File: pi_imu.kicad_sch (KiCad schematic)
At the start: 4 parts, among them J8 430450212, U10 4754, U6 MAX485, U8 RASPBERRY_PI_4B_4GB

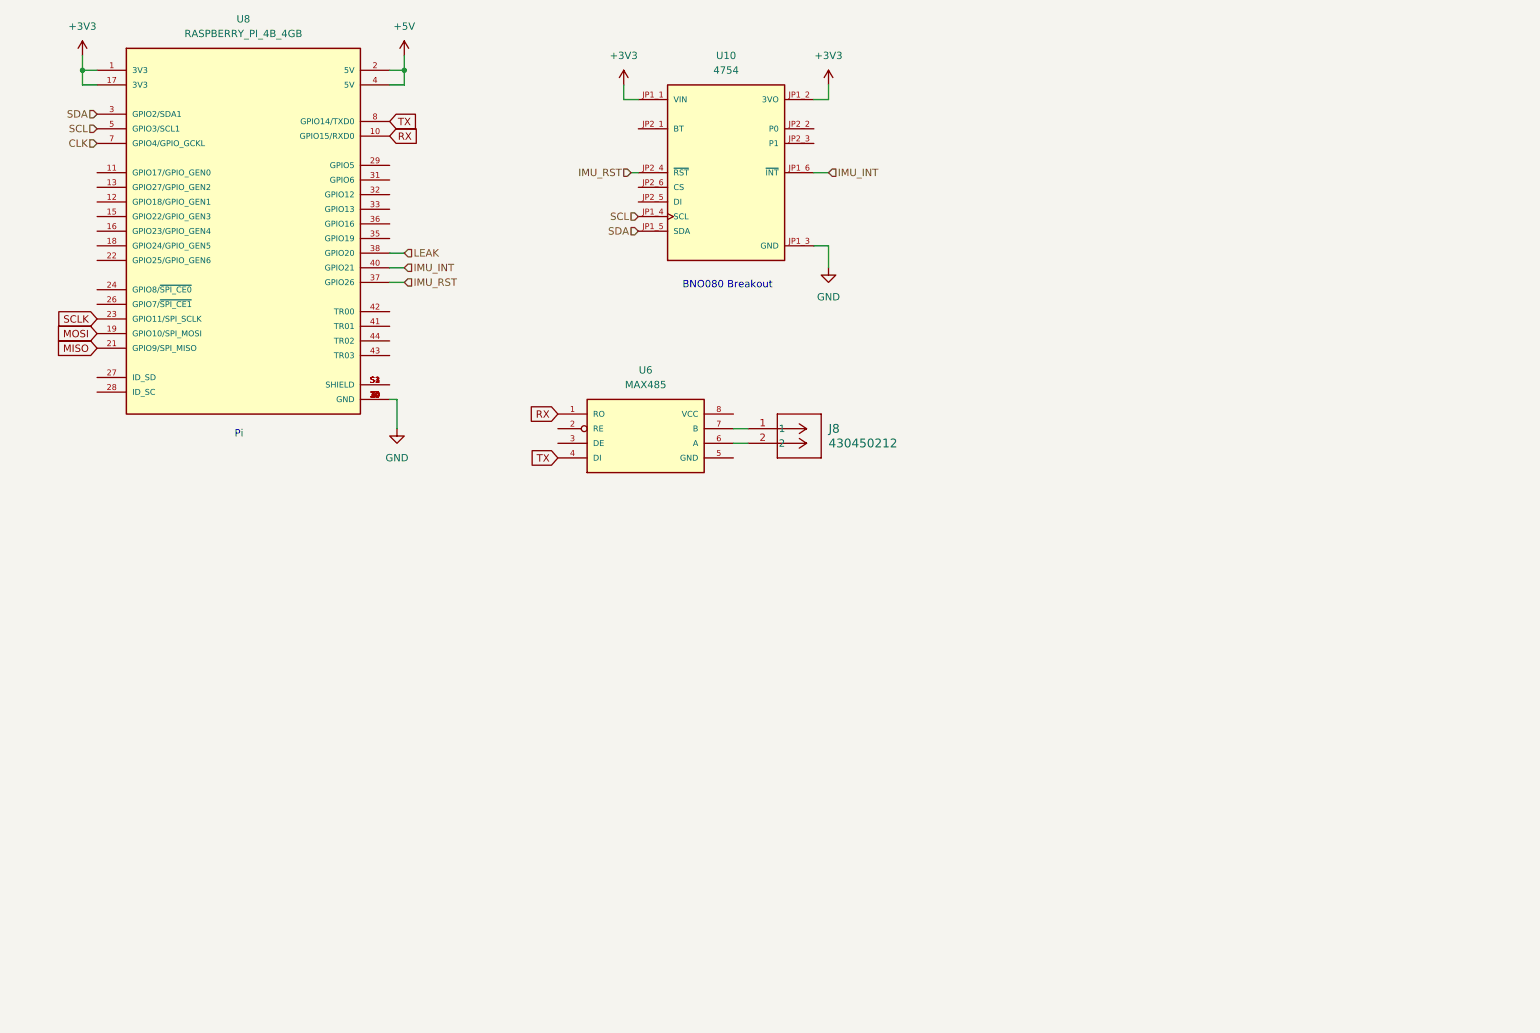
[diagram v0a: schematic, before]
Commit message: Added New Libraries and Schematic Updates
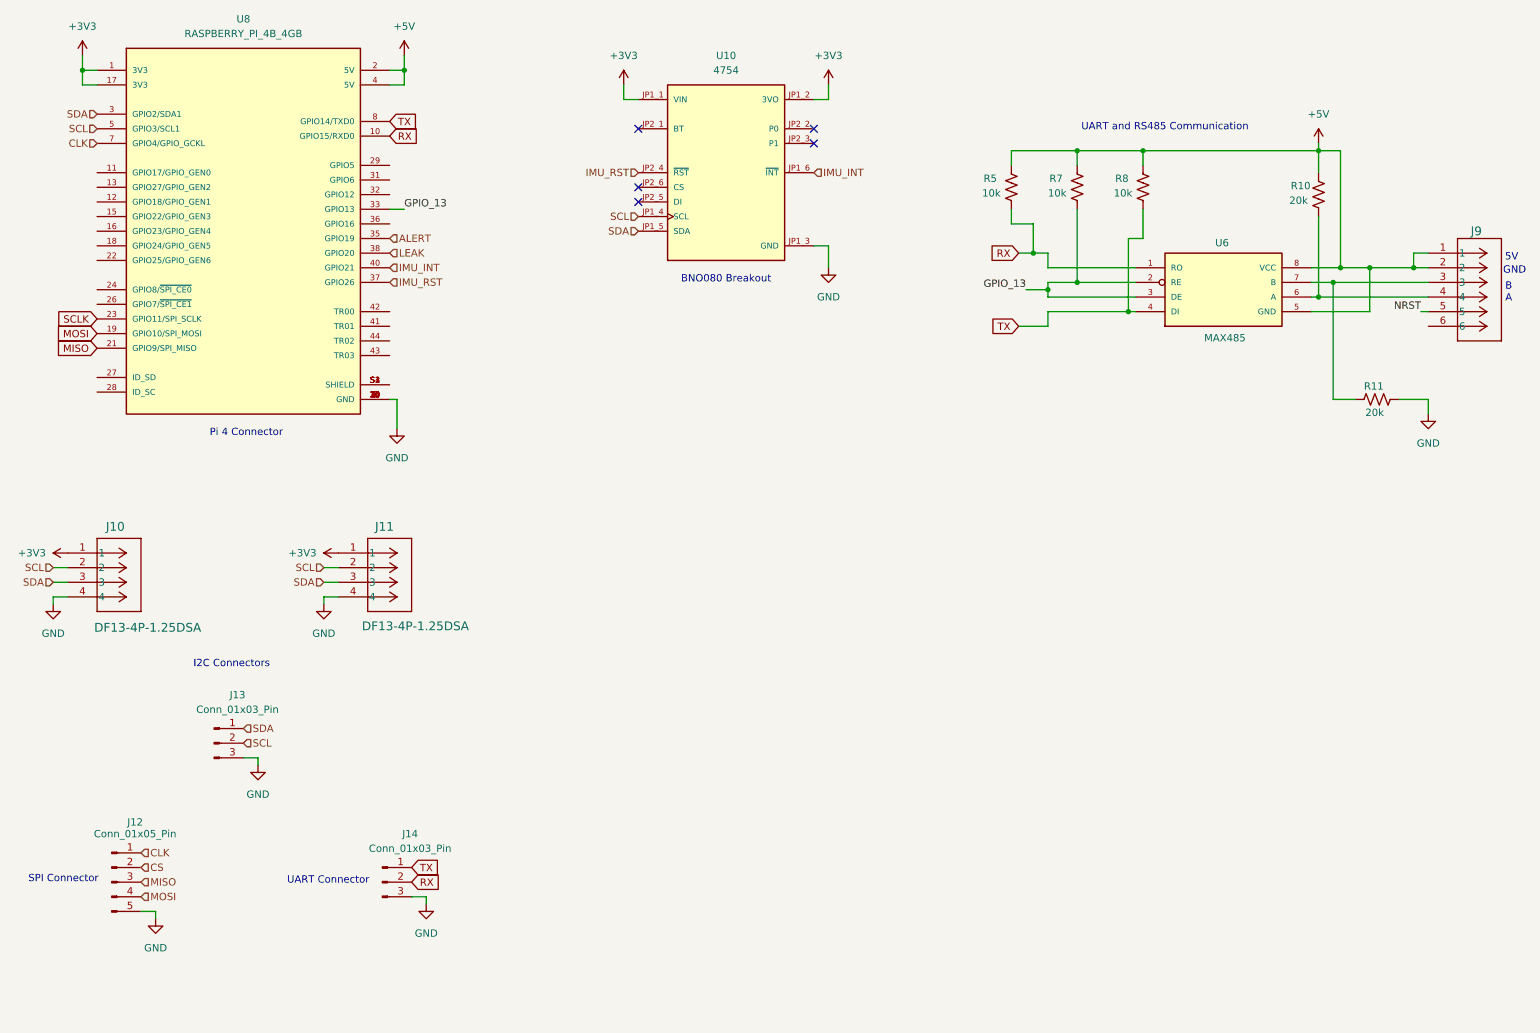
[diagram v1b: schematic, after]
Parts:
- removed J8: 430450212, symbol 0430450212:430450212
- added J10, J11: DF13-4P-1.25DSA, CON4_1X4_U_DF13, symbol DF13_4P_1_25DSA:DF13-4P-1.25DSA
- added J12: Conn_01x05_Pin, symbol Connector:Conn_01x05_Pin
- added J13, J14: Conn_01x03_Pin, symbol Connector:Conn_01x03_Pin
- added J9: 430450612, CON_430450612_MOL, symbol CON_430450612_MOL:430450612
- added R10, R11: 20k, symbol Device:R_US
- added R5, R7, R8: 10k, symbol Device:R_US
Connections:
- net +3V3: now also J10.1, J11.1
- net +5V: now also U6.5 (GND), U6.8 (VCC), J9.1, J9.2, R10.1, R5.1, R7.1, R8.1
- net CLK: now also J12.1 (Pin_1)
- net GND: now also J10.4, J11.4, J12.5 (Pin_5), J13.3 (Pin_3), J14.3 (Pin_3), R11.1
- net MISO: now also J12.3 (Pin_3)
- net MOSI: now also J12.4 (Pin_4)
- net RX: now also J14.2 (Pin_2), R5.2
- net SCL: now also J10.2, J11.2, J13.2 (Pin_2)
- net SDA: now also J10.3, J11.3, J13.1 (Pin_1)
- net TX: now also J14.1 (Pin_1), R8.2
- net GPIO_13: now reaches U6.2 (RE)
- net GPIO_13: now also U6.3 (DE), U8.33 (GPIO13), R7.2
- net at U6.6 (A): now also J9.4, R10.2
- net at U6.7 (B): now also J9.3, R11.2
- net ALERT: now reaches U8.35 (GPIO19)
- new net CS: J12.2 (Pin_2)
- new net NRST: J9.5
- no-connect marks 0 -> 5
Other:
- note added: "5V"
- note added: "B A"
- note added: "GND"
- note added: "I2C Connectors"
- note added: "Pi 4 Connector"
- note added: "SPI Connector"
- note added: "UART Connector"
- note added: "UART and RS485 Communication"
- note removed: "Pi"
- moved on the sheet: U6

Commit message: Root Update and Adding ISO Pt1
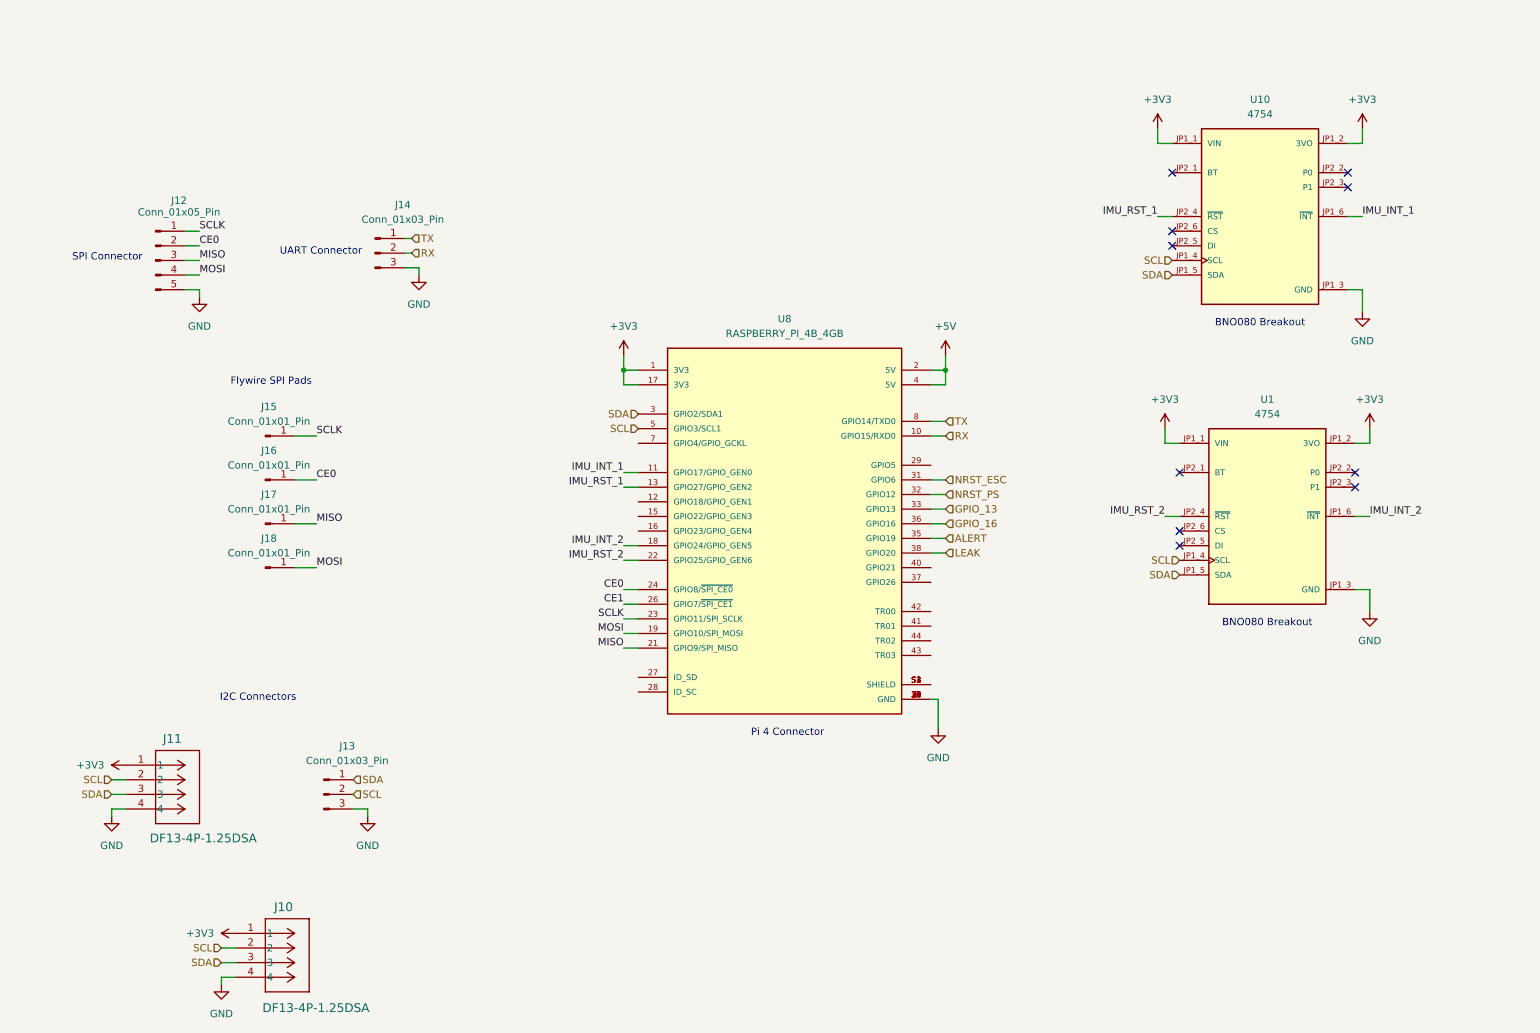
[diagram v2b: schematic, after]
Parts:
- removed J9: 430450612, CON_430450612_MOL, symbol CON_430450612_MOL:430450612
- removed R10, R11: 20k, symbol Device:R_US
- removed R5, R7, R8: 10k, symbol Device:R_US
- removed U6: MAX485, symbol MAX485:MAX485
- added J15, J16, J17, J18: Conn_01x01_Pin, symbol Connector:Conn_01x01_Pin
- added U1: 4754, 4754:MODULE_4754, symbol 4754:4754
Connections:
- net CS is gone; now on net CE0: J12.2 (Pin_2)
- net +3V3: now also U1.JP1_1 (VIN), U1.JP1_2 (3VO)
- net GND: now also U1.JP1_3 (GND)
- net MISO: now also J17.1 (Pin_1)
- net MOSI: now also J18.1 (Pin_1)
- net SCL: now also U1.JP1_4 (SCL)
- net SCLK: now also J12.1 (Pin_1), J15.1 (Pin_1)
- net SDA: now also U1.JP1_5 (SDA)
- net IMU_INT_1: now reaches U8.11 (GPIO17/GPIO_GEN0)
- net IMU_INT_1: now also U10.JP1_6 (~{INT})
- net IMU_RST_1: now reaches U8.13 (GPIO27/GPIO_GEN2)
- net IMU_RST_1: now also U10.JP2_4 (~{RST})
- net IMU_INT_2: now reaches U8.18 (GPIO24/GPIO_GEN5)
- net IMU_INT_2: now also U1.JP1_6 (~{INT})
- net IMU_RST_2: now reaches U8.22 (GPIO25/GPIO_GEN6)
- net IMU_RST_2: now also U1.JP2_4 (~{RST})
- net CE0: now reaches U8.24 (GPIO8/~{SPI_CE0})
- net CE0: now also J16.1 (Pin_1)
- net CE1: now reaches U8.26 (GPIO7/~{SPI_CE1})
- net NRST_ESC: now reaches U8.31 (GPIO6)
- net NRST_PS: now reaches U8.32 (GPIO12)
- net GPIO_16: now reaches U8.36 (GPIO16)
- net CLK: no longer names the net of U8.7 (GPIO4/GPIO_GCKL)
- net CLK: no longer J12.1 (Pin_1)
- net IMU_INT: no longer names the net of U8.40 (GPIO21)
- net IMU_INT: no longer U10.JP1_6 (~{INT})
- net IMU_RST: no longer names the net of U8.37 (GPIO26)
- net IMU_RST: no longer U10.JP2_4 (~{RST})
- no-connect marks 5 -> 10
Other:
- note added: "Flywire SPI Pads"
- note removed: "5V"
- note removed: "B A"
- note removed: "GND"
- note removed: "UART and RS485 Communication"
- moved on the sheet: J10, J11, J12, J13, J14, U10, U8

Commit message: Adding Libraries
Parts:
- added C12, C13: 10uF, symbol Device:C
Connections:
- net GPIO_16 is gone; now on net ALERT: U8.36 (GPIO16)
- net +3V3: now also C13.1
- net +5V: now also C12.1
- net ALERT: no longer U8.35 (GPIO19)
- net GND: now also C12.2, C13.2
- net IMU_INT_2: now also U8.12 (GPIO18/GPIO_GEN1); no longer U8.18 (GPIO24/GPIO_GEN5)
- net IMU_RST_2: now also U8.15 (GPIO22/GPIO_GEN3); no longer U8.22 (GPIO25/GPIO_GEN6)
- net LEAK: now also U8.35 (GPIO19); no longer U8.38 (GPIO20)
- net NRST_ESC: now also U8.29 (GPIO5); no longer U8.31 (GPIO6)
- net NRST_PS: now also U8.31 (GPIO6); no longer U8.32 (GPIO12)
- net GPIO_13 renamed TB_EN
- new net BKP_EN: U8.32 (GPIO12)
- no-connect marks 10 -> 12
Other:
- moved on the sheet: J10, J13

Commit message: Finalizing Schematic
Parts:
- added C15, C16: 10uF, symbol Device:C
- added R19, R20: 4.7k, symbol Device:R_US
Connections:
- net +3V3: now also C15.1, R19.1, R20.1
- net +5V: now also C12.2, C16.2; no longer C12.1
- net GND: now also C12.1, C15.2, C16.1; no longer C12.2
- net SCL: now also R19.2
- net SDA: now also R20.2
- net GPIO_23: now reaches U8.16 (GPIO23/GPIO_GEN4)
- net GPIO_24: now reaches U8.18 (GPIO24/GPIO_GEN5)
- net GPIO_25: now reaches U8.22 (GPIO25/GPIO_GEN6)
- net GPIO_26: now reaches U8.37 (GPIO26)
- net GPIO_20: now reaches U8.38 (GPIO20)
- net GPIO_21: now reaches U8.40 (GPIO21)
- net GPIO_4: now reaches U8.7 (GPIO4/GPIO_GCKL)
- no-connect marks 12 -> 17
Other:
- note added: "BNO080 IMU Breakouts"
- note added: "I2C Pull Up Resistors"
- note removed: "BNO080 Breakout"
- moved on the sheet: J10, J11, J12, J13, J14, J15, J16, J17, J18, U1, U10, U8

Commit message: Final Schematic Update
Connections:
- net +3V3: no longer U1.JP1_2 (3VO), U10.JP1_2 (3VO)
- net CE1: no longer names the net of U8.26 (GPIO7/~{SPI_CE1})
- net GPIO_20: no longer names the net of U8.38 (GPIO20)
- net GPIO_21: no longer names the net of U8.40 (GPIO21)
- net GPIO_23: no longer names the net of U8.16 (GPIO23/GPIO_GEN4)
- net GPIO_24: no longer names the net of U8.18 (GPIO24/GPIO_GEN5)
- net GPIO_25: no longer names the net of U8.22 (GPIO25/GPIO_GEN6)
- net GPIO_26: no longer names the net of U8.37 (GPIO26)
- net GPIO_4: no longer names the net of U8.7 (GPIO4/GPIO_GCKL)
- no-connect marks 17 -> 27
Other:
- moved on the sheet: C12, C13, C15, C16, J10, J11, J12, J13, J14, J15, J16, J17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

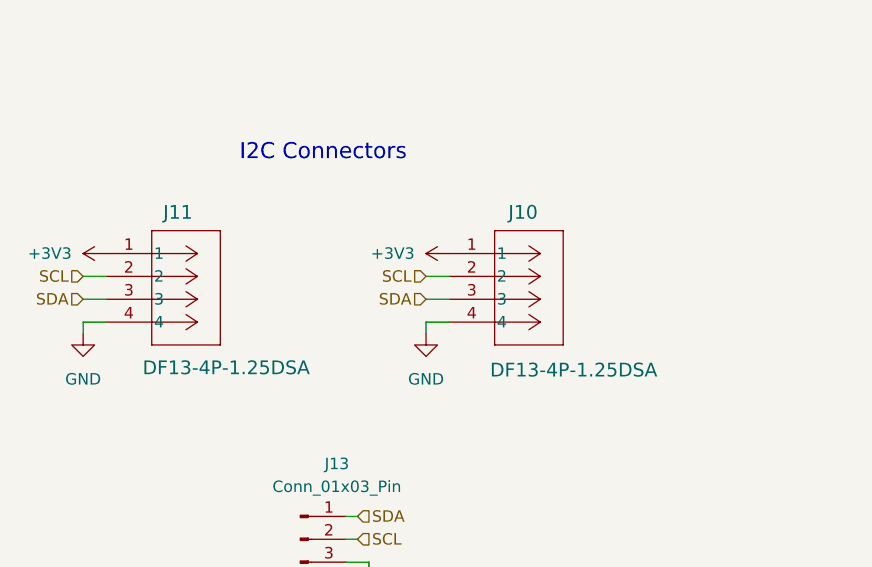
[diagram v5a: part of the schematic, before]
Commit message: Sensor Connector Update
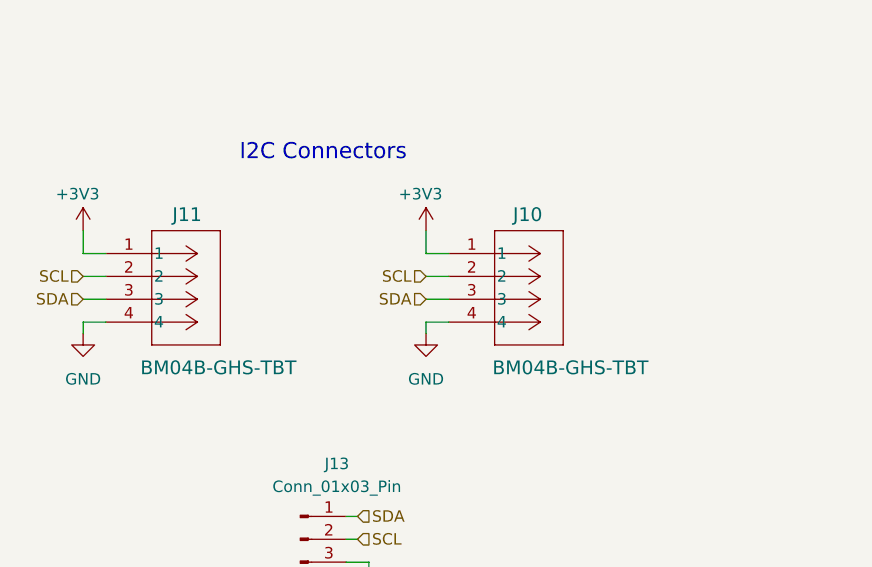
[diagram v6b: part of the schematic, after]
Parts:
- removed J10, J11: DF13-4P-1.25DSA, CON4_1X4_U_DF13, symbol DF13_4P_1_25DSA:DF13-4P-1.25DSA
- added J10, J11: BM04B-GHS-TBT, CONN_BM04B-GHS-TBT_JST, symbol BM04B_GHS_TBT:BM04B-GHS-TBT
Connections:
- net +3V3: now also J10.1, J11.1
- net GND: now also J10.4, J11.4
- net SCL: now also J10.2, J11.2
- net SDA: now also J10.3, J11.3

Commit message: Pre-Toolbox Final
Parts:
- removed R19, R20: 4.7k, symbol Device:R_US
- C12, C13, C15, C16: footprint (none) -> Capacitor_SMD:C_0805_2012Metric_Pad1.18x1.45mm_HandSolder
- J10, J11: footprint CONN_BM04B-GHS-TBT_JST -> Connector_JST:JST_GH_BM04B-GHS-TBT_1x04-1MP_P1.25mm_Vertical
- J12, J13: footprint (none) -> Connector_PinHeader_2.54mm:PinHeader_1x05_P2.54mm_Vertical
- J14: footprint (none) -> Connector_PinHeader_2.54mm:PinHeader_1x03_P2.54mm_Vertical
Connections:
- net BKP_EN: now also U8.35 (GPIO19); no longer U8.32 (GPIO12)
- net LEAK: now also U8.16 (GPIO23/GPIO_GEN4); no longer U8.35 (GPIO19)
- net TB_EN: now also U8.38 (GPIO20); no longer U8.33 (GPIO13)
- new net RX_TB: U8.33 (GPIO13)
- new net TX_TB: U8.32 (GPIO12)
- no-connect marks 27 -> 25
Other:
- note removed: "I2C Pull Up Resistors"

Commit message: Finalized Footprints
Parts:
- removed J15, J16, J17, J18: Conn_01x01_Pin, symbol Connector:Conn_01x01_Pin
- added J9: Conn_01x04_Pin, Connector_PinHeader_2.54mm:PinHeader_1x04_P2.54mm_Vertical, symbol Connector:Conn_01x04_Pin
- C12, C13, C15, C16: footprint Capacitor_SMD:C_0805_2012Metric_Pad1.18x1.45mm_HandSolder -> Capacitor_SMD:C_0603_1608Metric_Pad1.08x0.95mm_HandSolder
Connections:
- net CE0: now also J9.2 (Pin_2)
- net MISO: now also J9.3 (Pin_3)
- net MOSI: now also J9.4 (Pin_4)
- net SCLK: now also J9.1 (Pin_1)
- net ISO_FLT: now reaches U8.18 (GPIO24/GPIO_GEN5)
- net NRST_TB: now reaches U8.40 (GPIO21)
- no-connect marks 25 -> 23
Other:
- moved on the sheet: J14
